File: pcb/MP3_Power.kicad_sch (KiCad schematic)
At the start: 0 parts

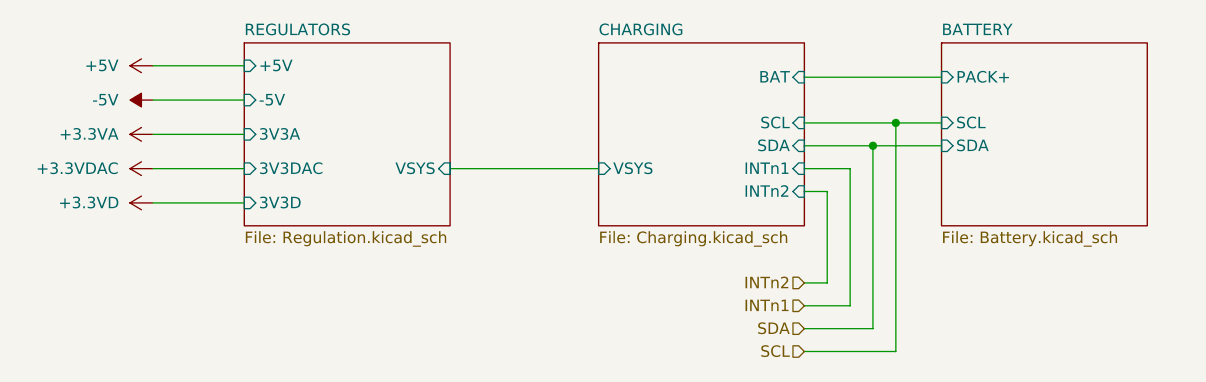
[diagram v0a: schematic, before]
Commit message: latest updates to schematic, changed to continuous ground
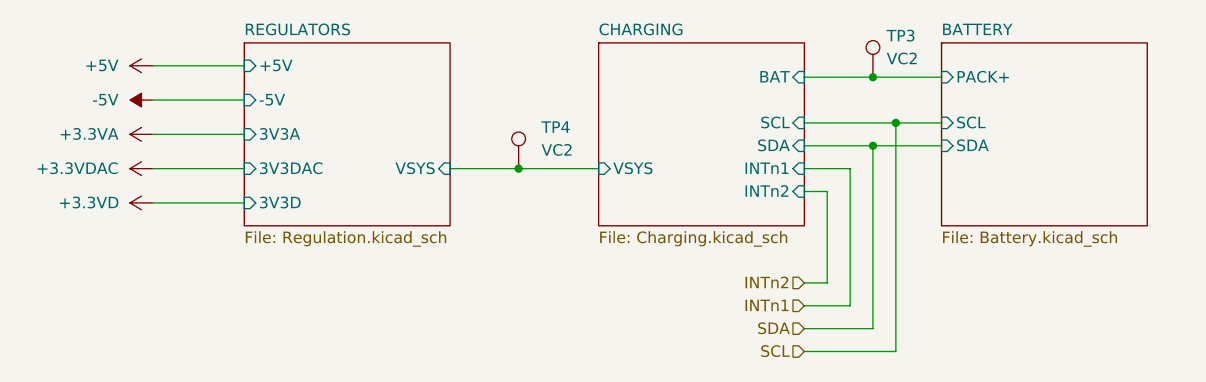
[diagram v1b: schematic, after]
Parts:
- added TP3, TP4: VC2, TestPoint:TestPoint_Pad_3.0x3.0mm, symbol Connector:TestPoint
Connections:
- net BATTERY/PACK+: now also TP3.1
- net CHARGING/VSYS: now also TP4.1
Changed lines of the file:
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@@
+	)
+	(junction
+		(at 118.11 68.58)
+		(diameter 0)
+		(color 0 0 0 0)
 	)
 	(junction
@@
 		(color 0 0 0 0)
 	)
+	(junction
+		(at 157.48 58.42)
+		(diameter 0)
+		(color 0 0 0 0)
+	)
 	(wire
 		(pts
@@
 	(wire
 		(pts
+			(xy 118.11 68.58) (xy 127 68.58)
+		)
+		(stroke
+			(width 0.762)
+			(type default)
+		)
+	)
+	(wire
+		(pts
 			(xy 160.02 88.9) (xy 149.86 88.9)
 		)
@@
 	(wire
 		(pts
-			(xy 149.86 58.42) (xy 165.1 58.42)
+			(xy 149.86 58.42) (xy 157.48 58.42)
 		)
 		(stroke
@@
 	(wire
 		(pts
-			(xy 110.49 68.58) (xy 127 68.58)
+			(xy 110.49 68.58) (xy 118.11 68.58)
 		)
 		(stroke
@@
 		(stroke
 			(width 0)
+			(type default)
+		)
+	)
+	(wire
+		(pts
+			(xy 157.48 58.42) (xy 165.1 58.42)
+		)
+		(stroke
+			(width 0.762)
 			(type default)
 		)
@@
 	)
 	(symbol
+		(lib_id "Connector:TestPoint")
+		(at 157.48 58.42 0)
+		(unit 1)
+		(exclude_from_sim no)
+		(in_bom yes)
+		(on_board yes)
+		(dnp no)
+		(property "Reference" "TP3"
+			(at 159.004 53.848 0)
+			(effects
+				(font
+					(size 1.27 1.27)
+				)
+				(justify left)
+			)
+		)
+		(property "Value" "VC2"
+			(at 159.004 56.388 0)
+			(effects
+				(font
+					(size 1.27 1.27)
+				)
+				(justify left)
+			)
+		)
+		(property "Footprint" "TestPoint:TestPoint_Pad_3.0x3.0mm"
+			(at 162.56 58.42 0)
+			(effects
+				(font
+					(size 1.27 1.27)
+				)
+				(hide yes)
+			)
+		)
+		(property "Datasheet" "~"
+			(at 162.56 58.42 0)
+			(effects
+				(font
+					(size 1.27 1.27)
+				)
+				(hide yes)
+			)
+		)
+		(property "Description" "test point"
+			(at 157.48 58.42 0)
+			(effects
+				(font
+					(size 1.27 1.27)
+				)
+				(hide yes)
+			)
+		)
+		(pin "1"
+		)
+		(instances
+			(project "pcb"
+				(path "/0eb23f11-7b6a-445b-9941-73800592c9c0/a374f7f9-840e-4f0c-b221-b48771a4edc6"
+					(reference "TP3")
+					(unit 1)
+				)
+			)
+		)
+	)
+	(symbol
 		(lib_id "power:+3.3VA")
 		(at 77.47 64.77 90)
@@
 					(unit 1)
 				)
+			)
+		)
+	)
+	(symbol
+		(lib_id "Connector:TestPoint")
+		(at 118.11 68.58 0)
+		(unit 1)
+		(exclude_from_sim no)
+		(in_bom yes)
+		(on_board yes)
+		(dnp no)
+		(fields_autoplaced yes)
+		(property "Reference" "TP4"
+			(at 120.65 64.0079 0)
+			(effects
+				(font
+					(size 1.27 1.27)
+				)
+				(justify left)
+			)
+		)
+		(property "Value" "VC2"
+			(at 120.65 66.5479 0)
+			(effects
+				(font
+					(size 1.27 1.27)
+				)
+				(justify left)
+			)
+		)
+		(property "Footprint" "TestPoint:TestPoint_Pad_3.0x3.0mm"
+			(at 123.19 68.58 0)
+			(effects
+				(font
+					(size 1.27 1.27)
+				)
+				(hide yes)
+			)
+		)
+		(property "Datasheet" "~"
+			(at 123.19 68.58 0)
+			(effects
+				(font
+					(size 1.27 1.27)
+				)
+				(hide yes)
+			)
+		)
+		(property "Description" "test point"
+			(at 118.11 68.58 0)
+			(effects
+				(font
+					(size 1.27 1.27)
+				)
+				(hide yes)
+			)
+		)
+		(pin "1"
+		)
+		(instances
+			(project "pcb"
+				(path "/0eb23f11-7b6a-445b-9941-73800592c9c0/a374f7f9-840e-4f0c-b221-b48771a4edc6"
+					(reference "TP4")
+					(unit 1)
+				)
